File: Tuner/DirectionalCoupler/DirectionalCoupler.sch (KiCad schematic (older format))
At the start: 71 parts, among them J1 Conn_01x02, J10 Conn_01x01, J11 Conn_01x01, J12 Conn_01x01, J13 Conn_01x01, J14 Conn_01x01, J15 Conn_01x01, J16 Conn_01x01, J17 Barrel_Jack, J18 Conn_Coaxial, J19 Conn_01x02, J2 Conn_01x02, J20 Conn_Coaxial, J21 Conn_01x01, J22 Conn_01x01, J23 Conn_01x01, J24 Conn_01x01, J25 Conn_01x01, J26 Conn_01x01, J27 Conn_01x01, J28 Conn_01x01, J29 Conn_01x01, J3 Conn_Coaxial, J30 Conn_01x01, J31 Conn_01x01, J32 Conn_01x01, J33 Conn_01x03, J4 Conn_Coaxial, J5 Conn_01x01, J6 Conn_01x01, J7 Conn_01x01, J8 Conn_01x01, J9 Conn_01x01

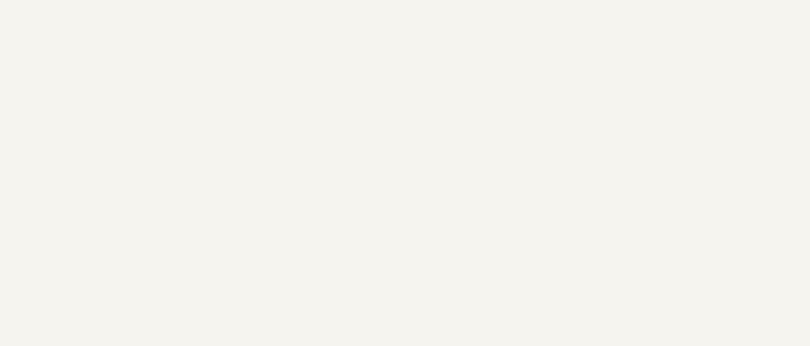
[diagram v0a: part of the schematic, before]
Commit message: Change named to DirectionalCoupler, fixed order of two pins in QuadCoupler
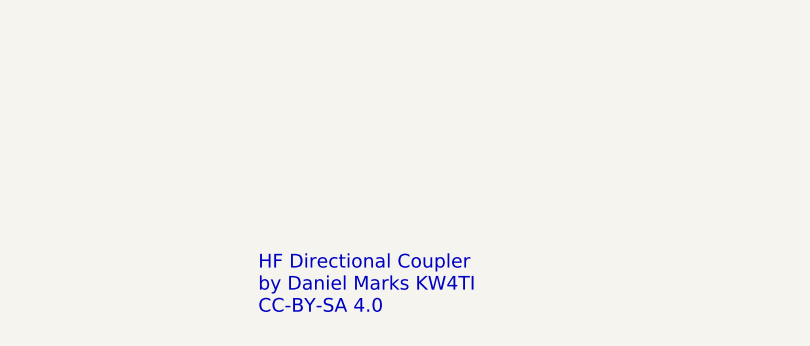
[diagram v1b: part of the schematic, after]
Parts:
- F1: footprint TandemMatch:SL506Pfuseholder -> DirectionalCoupler:SL506Pfuseholder
- J18, J20, J3, J4: footprint TandemMatch:bnc_90_1-1337543-0_pad_combo -> DirectionalCoupler:bnc_90_1-1337543-0_pad_combo
- L1: footprint TandemMatch:BigRFChokeInductor -> DirectionalCoupler:BigRFChokeInductor
- R1, R2, R3, R4: footprint TandemMatch:R_Axial_DIN0309_L9.0mm_D3.2mm_P12.70mm_Horizontal -> DirectionalCoupler:R_Axial_DIN0309_L9.0mm_D3.2mm_P12.70mm_Horizontal
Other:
- note added: "HF Directional Coupler\nby Daniel Marks KW4TI\nCC-BY-SA 4.0\n"
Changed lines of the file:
@@
 LIBS:contrib
 LIBS:valves
-LIBS:TandemMatch-cache
+LIBS:DirectionalCoupler-cache
 EELAYER 25 0
 EELAYER END
@@
 F 0 "J3" H 1910 2920 50  0000 C CNN
 F 1 "Conn_Coaxial" V 2015 2800 50  0000 C CNN
-F 2 "TandemMatch:bnc_90_1-1337543-0_pad_combo" H 1900 2800 50  0001 C CNN
+F 2 "DirectionalCoupler:bnc_90_1-1337543-0_pad_combo" H 1900 2800 50  0001 C CNN
 F 3 "" H 1900 2800 50  0001 C CNN
 	1    1900 2800
@@
 F 0 "J18" H 5760 2920 50  0000 C CNN
 F 1 "Conn_Coaxial" V 5865 2800 50  0000 C CNN
-F 2 "TandemMatch:bnc_90_1-1337543-0_pad_combo" H 5750 2800 50  0001 C CNN
+F 2 "DirectionalCoupler:bnc_90_1-1337543-0_pad_combo" H 5750 2800 50  0001 C CNN
 F 3 "" H 5750 2800 50  0001 C CNN
 	1    5750 2800
@@
 F 0 "J4" H 1960 4420 50  0000 C CNN
 F 1 "Conn_Coaxial" V 2065 4300 50  0000 C CNN
-F 2 "TandemMatch:bnc_90_1-1337543-0_pad_combo" H 1950 4300 50  0001 C CNN
+F 2 "DirectionalCoupler:bnc_90_1-1337543-0_pad_combo" H 1950 4300 50  0001 C CNN
 F 3 "" H 1950 4300 50  0001 C CNN
 	1    1950 4300
@@
 F 0 "J20" H 5860 5070 50  0000 C CNN
 F 1 "Conn_Coaxial" V 5965 4950 50  0000 C CNN
-F 2 "TandemMatch:bnc_90_1-1337543-0_pad_combo" H 5850 4950 50  0001 C CNN
+F 2 "DirectionalCoupler:bnc_90_1-1337543-0_pad_combo" H 5850 4950 50  0001 C CNN
 F 3 "" H 5850 4950 50  0001 C CNN
 	1    5850 4950
@@
 F 0 "R1" V 2430 1650 50  0000 C CNN
 F 1 "100R" V 2350 1650 50  0000 C CNN
-F 2 "TandemMatch:R_Axial_DIN0309_L9.0mm_D3.2mm_P12.70mm_Horizontal" V 2280 1650 50  0001 C CNN
+F 2 "DirectionalCoupler:R_Axial_DIN0309_L9.0mm_D3.2mm_P12.70mm_Horizontal" V 2280 1650 50  0001 C CNN
 F 3 "" H 2350 1650 50  0001 C CNN
 	1    2350 1650
@@
 F 0 "R2" V 2630 1650 50  0000 C CNN
 F 1 "100R" V 2550 1650 50  0000 C CNN
-F 2 "TandemMatch:R_Axial_DIN0309_L9.0mm_D3.2mm_P12.70mm_Horizontal" V 2480 1650 50  0001 C CNN
+F 2 "DirectionalCoupler:R_Axial_DIN0309_L9.0mm_D3.2mm_P12.70mm_Horizontal" V 2480 1650 50  0001 C CNN
 F 3 "" H 2550 1650 50  0001 C CNN
 	1    2550 1650
@@
 F 0 "R3" V 5030 1650 50  0000 C CNN
 F 1 "100R" V 4950 1650 50  0000 C CNN
-F 2 "TandemMatch:R_Axial_DIN0309_L9.0mm_D3.2mm_P12.70mm_Horizontal" V 4880 1650 50  0001 C CNN
+F 2 "DirectionalCoupler:R_Axial_DIN0309_L9.0mm_D3.2mm_P12.70mm_Horizontal" V 4880 1650 50  0001 C CNN
 F 3 "" H 4950 1650 50  0001 C CNN
 	1    4950 1650
@@
 F 0 "R4" V 5230 1650 50  0000 C CNN
 F 1 "100R" V 5150 1650 50  0000 C CNN
-F 2 "TandemMatch:R_Axial_DIN0309_L9.0mm_D3.2mm_P12.70mm_Horizontal" V 5080 1650 50  0001 C CNN
+F 2 "DirectionalCoupler:R_Axial_DIN0309_L9.0mm_D3.2mm_P12.70mm_Horizontal" V 5080 1650 50  0001 C CNN
 F 3 "" H 5150 1650 50  0001 C CNN
 	1    5150 1650
@@
 F 0 "L1" V 5750 4550 50  0000 C CNN
 F 1 "L" V 5875 4550 50  0000 C CNN
-F 2 "TandemMatch:BigRFChokeInductor" H 5800 4550 50  0001 C CNN
+F 2 "DirectionalCoupler:BigRFChokeInductor" H 5800 4550 50  0001 C CNN
 F 3 "" H 5800 4550 50  0001 C CNN
 	1    5800 4550
@@
 F 0 "F1" V 6430 4300 50  0000 C CNN
 F 1 "Keystone 3544-2 / SL-506P" H 6700 4450 50  0000 C CNN
-F 2 "TandemMatch:SL506Pfuseholder" V 6280 4300 50  0001 C CNN
+F 2 "DirectionalCoupler:SL506Pfuseholder" V 6280 4300 50  0001 C CNN
 F 3 "" H 6350 4300 50  0001 C CNN
 	1    6350 4300
@@
 	5600 2800 5550 2800
 Connection ~ 5300 2800
+Text Notes 7450 6950 0    60   ~ 0
+HF Directional Coupler\nby Daniel Marks KW4TI\nCC-BY-SA 4.0\n
 $EndSCHEMATC

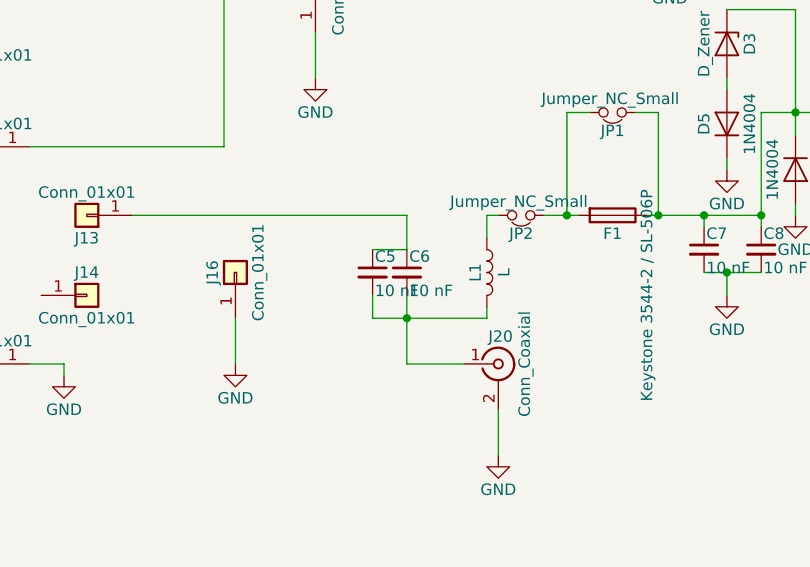
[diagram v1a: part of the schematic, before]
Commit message: Added OptoisolatedRelay
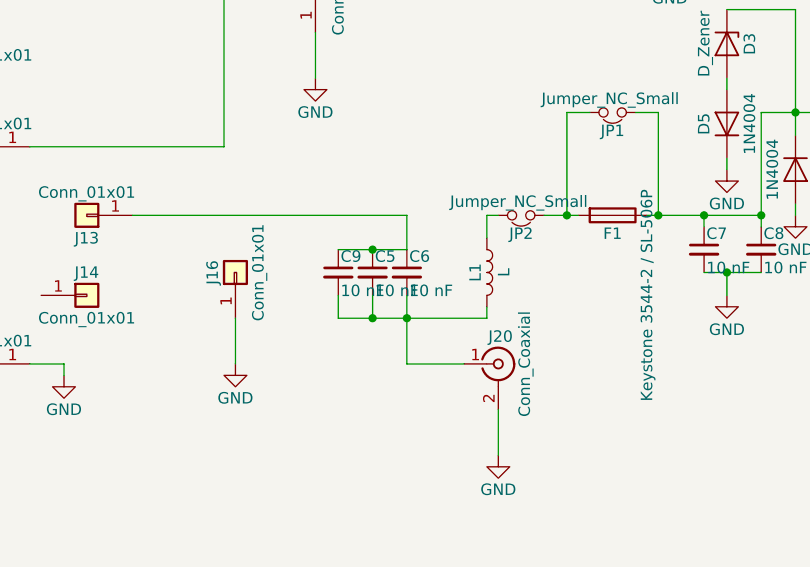
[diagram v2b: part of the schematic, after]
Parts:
- added C9: 10 nF, Capacitors_THT:C_Disc_D5.0mm_W2.5mm_P5.00mm, symbol C_Small
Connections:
- net at C5.2, C6.2, J20.1 (In)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: now also C9.2
- net at C5.1, C6.1, J13.1 (Pin_1): now also C9.1
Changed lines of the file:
@@
 	5450 4650 5450 4950
 Wire Wire Line
-	5300 4450 5450 4450
+	5150 4450 5450 4450
 Wire Wire Line
 	5450 4450 5450 4300
@@
 	5300 4650 5300 4750
 Wire Wire Line
-	5300 4750 5800 4750
+	5150 4750 5800 4750
 Connection ~ 5450 4750
 Wire Wire Line
@@
 Text Notes 7450 6950 0    60   ~ 0
 HF Directional Coupler\nby Daniel Marks KW4TI\nCC-BY-SA 4.0\n
+$Comp
+L C_Small C9
+U 1 1 5CB0A1E1
+P 5150 4550
+F 0 "C9" H 5160 4620 50  0000 L CNN
+F 1 "10 nF" H 5160 4470 50  0000 L CNN
+F 2 "Capacitors_THT:C_Disc_D5.0mm_W2.5mm_P5.00mm" H 5150 4550 50  0001 C CNN
+F 3 "" H 5150 4550 50  0001 C CNN
+	1    5150 4550
+	1    0    0    -1
+$EndComp
+Connection ~ 5300 4450
+Wire Wire Line
+	5150 4650 5150 4750
+Connection ~ 5300 4750
 $EndSCHEMATC
